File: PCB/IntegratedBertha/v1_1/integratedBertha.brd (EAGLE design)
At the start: 108.1 x 84.6 mm, 100 parts, among them CON1 SPI, IC1 REG1117, IC2 AD8223, J7 22--02, Q1 BSP75, Q2 BSP75, Q4 BSP75, Q5 BSP75, Q6 BSP75, Q7 IRF3704S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

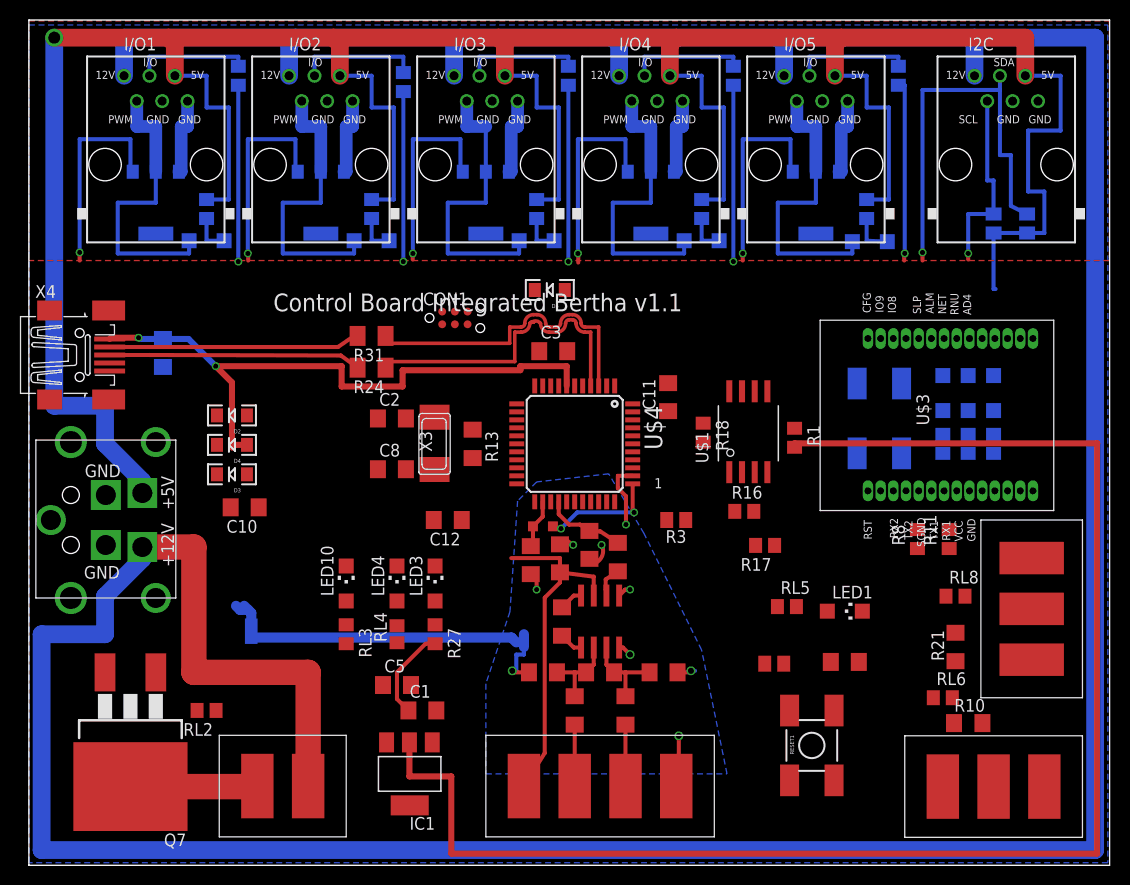
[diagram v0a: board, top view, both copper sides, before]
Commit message: routed anemometer and integrated bertha with ground planes and separate analog and digital ground. ready for fabrication
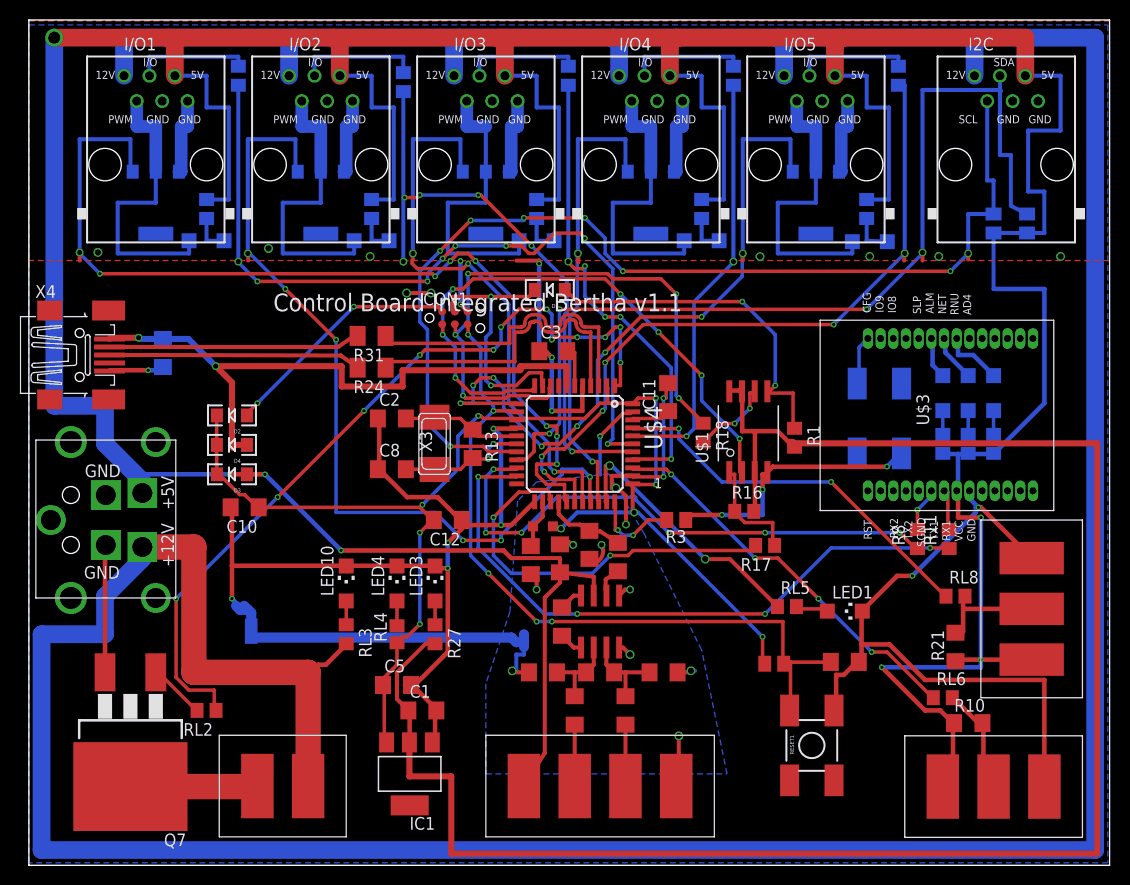
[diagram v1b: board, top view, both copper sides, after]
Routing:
- net GND: track 43.8 -> 284.9 mm, vias 0 -> 25
- net +5V: track 342.8 -> 470.7 mm, vias 1 -> 7
- net +5V/1: track 11.8 -> 130.1 mm, vias 2 -> 9
- net SCL: track 19.0 -> 105.7 mm, vias 1 -> 8
- net D7*: track 0.00 -> 81.5 mm, vias 0 -> 12
- net RESET: track 0.00 -> 75.5 mm, vias 0 -> 5
- net D6*: track 20.8 -> 95.0 mm, vias 1 -> 8
- net TX: track 0.00 -> 63.6 mm, vias 0 -> 4
- net A3: track 17.8 -> 81.0 mm, vias 1 -> 8
- net D10*: track 20.4 -> 83.0 mm, vias 1 -> 6
- net MISO: track 0.00 -> 60.6 mm, vias 0 -> 7
- net SCK: track 0.00 -> 59.9 mm, vias 0 -> 5
- net SDA: track 40.7 -> 98.0 mm, vias 1 -> 4
- net RX: track 0.00 -> 56.1 mm, vias 0 -> 6
- net D8*: track 18.2 -> 72.9 mm, vias 1 -> 6
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
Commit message: integratedBertha v1.1: adjusted labels to good position. Anemometer: added ferrite bead for vcc decoupling and ground line.
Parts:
- renumbered LED1 to BLINK, LED10 to 12V-OK, LED3 to 3.3V-OK, LED4 to 5V-OK
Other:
- board text added: "Integrated Bertha v1.1 Control Board"
- board text removed: "Control Board Integrated Bertha v1.1"
- board text removed: "LINKLED"
- board text removed: "USB"

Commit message: changed some labels, corrected C16 value in bertha. created BOM
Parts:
- C16: value 100uF -> 100nF
